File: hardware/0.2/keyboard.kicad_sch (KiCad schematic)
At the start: 324 parts, among them J1 USB_C_Receptacle_USB2.0, J2 SWD, J3 SPARE, Q1 2N7002, Q2 DTC123J, SW1 RotaryEncoder_Switch, SW10 KEYSW, SW100 KEYSW, SW101 KEYSW, SW102 KEYSW, SW103 KEYSW, SW104 KEYSW, SW105 KEYSW, SW106 KEYSW, SW107 KEYSW, SW108 KEYSW, SW109 KEYSW, SW11 KEYSW, SW110 KEYSW, SW111 KEYSW, SW112 KEYSW, SW113 KEYSW, SW114 KEYSW, SW115 KEYSW, SW116 KEYSW, SW117 KEYSW, SW118 KEYSW, SW119 KEYSW, SW12 KEYSW, SW120 KEYSW, SW121 KEYSW, SW122 KEYSW, SW123 KEYSW, SW124 RotaryEncoder_Switch, SW125 KEYSW, SW126 KEYSW, SW127 KEYSW, SW128 KEYSW, SW129 KEYSW, SW13 KEYSW, SW14 KEYSW, SW15 KEYSW, SW16 KEYSW, SW17 KEYSW, SW18 KEYSW, SW19 KEYSW, SW2 KEYSW, SW20 KEYSW, SW21 KEYSW, SW22 KEYSW, SW23 KEYSW, SW24 KEYSW, SW25 KEYSW, SW26 KEYSW, SW27 KEYSW, SW28 KEYSW, SW29 KEYSW, SW3 KEYSW, SW30 KEYSW, SW31 KEYSW, SW32 KEYSW, SW33 KEYSW, SW34 KEYSW, SW35 KEYSW, SW36 KEYSW, SW37 KEYSW, SW38 KEYSW, SW39 KEYSW, SW4 KEYSW, SW40 KEYSW, SW41 KEYSW, SW42 KEYSW, SW43 KEYSW, SW44 KEYSW, SW45 KEYSW, SW46 KEYSW, SW47 KEYSW, SW48 KEYSW, SW49 KEYSW, SW5 KEYSW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

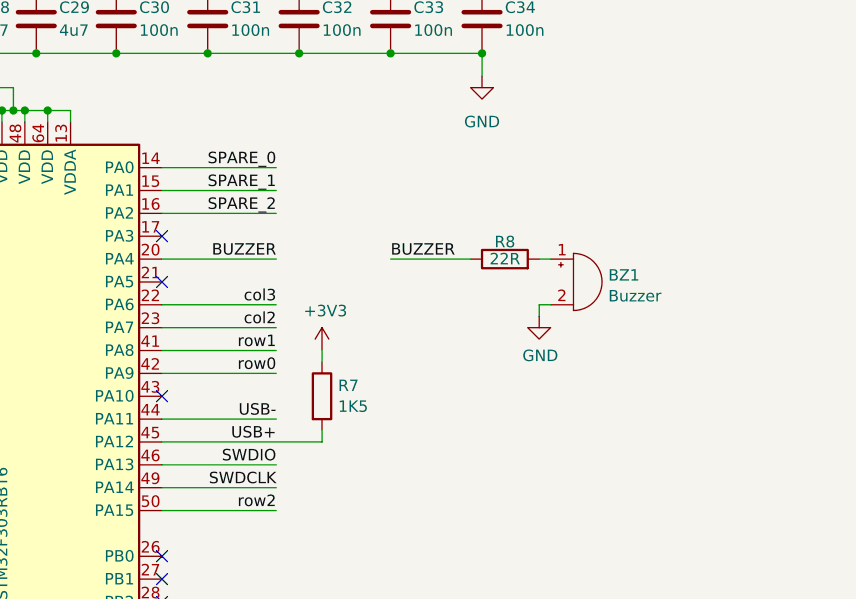
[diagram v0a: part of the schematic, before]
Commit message: update top layer dxf and make piezo louder
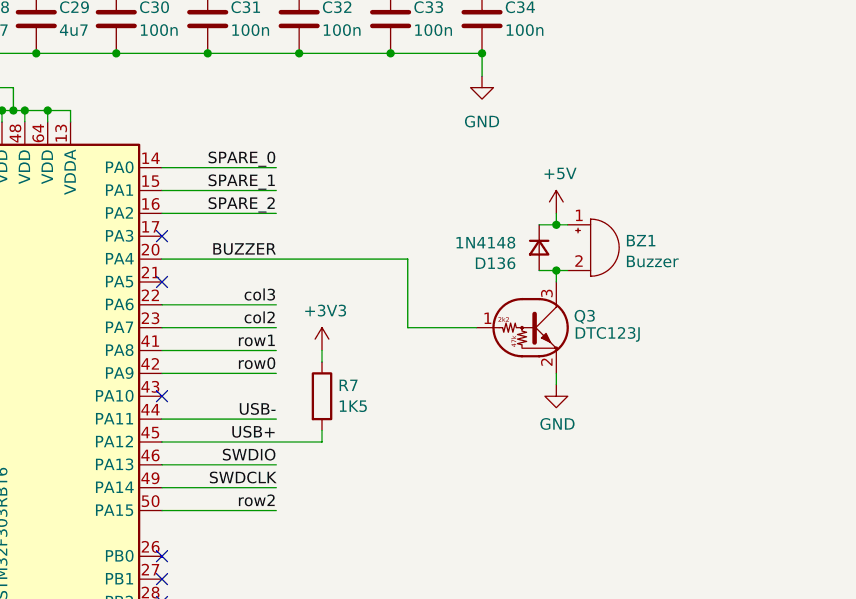
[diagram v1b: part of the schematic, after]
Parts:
- removed R8: 22R, Resistor_SMD:R_0603_1608Metric, symbol Device:R
- added D136: 1N4148, Diode_SMD:D_SOD-123, symbol Device:D_Small
- added Q3: DTC123J, Package_TO_SOT_SMD:SOT-23, symbol Transistor_BJT:DTC123J
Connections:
- net +5V: now also BZ1.1 (-), D136.1 (K)
- net BUZZER: now also Q3.1 (B)
- net GND: now also Q3.2 (E); no longer BZ1.2 (+)
- new net: BZ1.2 (+), D136.2 (A), Q3.3 (C)
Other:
- moved on the sheet: BZ1
